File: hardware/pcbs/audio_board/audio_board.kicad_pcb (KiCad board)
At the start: 4 copper layers, 152 x 117.3 mm, 135 parts, among them J1 I2C, J10 Stereo Line-in, J2 Conn_01x08, J3 NC3MAH, J4 AudioJack3, J5 NC3MAH, J6 NC3FAH1, J7 NC3FAH1, J8 NC3FAH1, J9 DECT, Q1 S8050, Q6 2N7002, Q7 SI2309CDS-T1-GE3, U2 LP5907MFX-3.3, U3 LM5158, U4 TAD5242, U5 TAD5242, U6 TAA3040

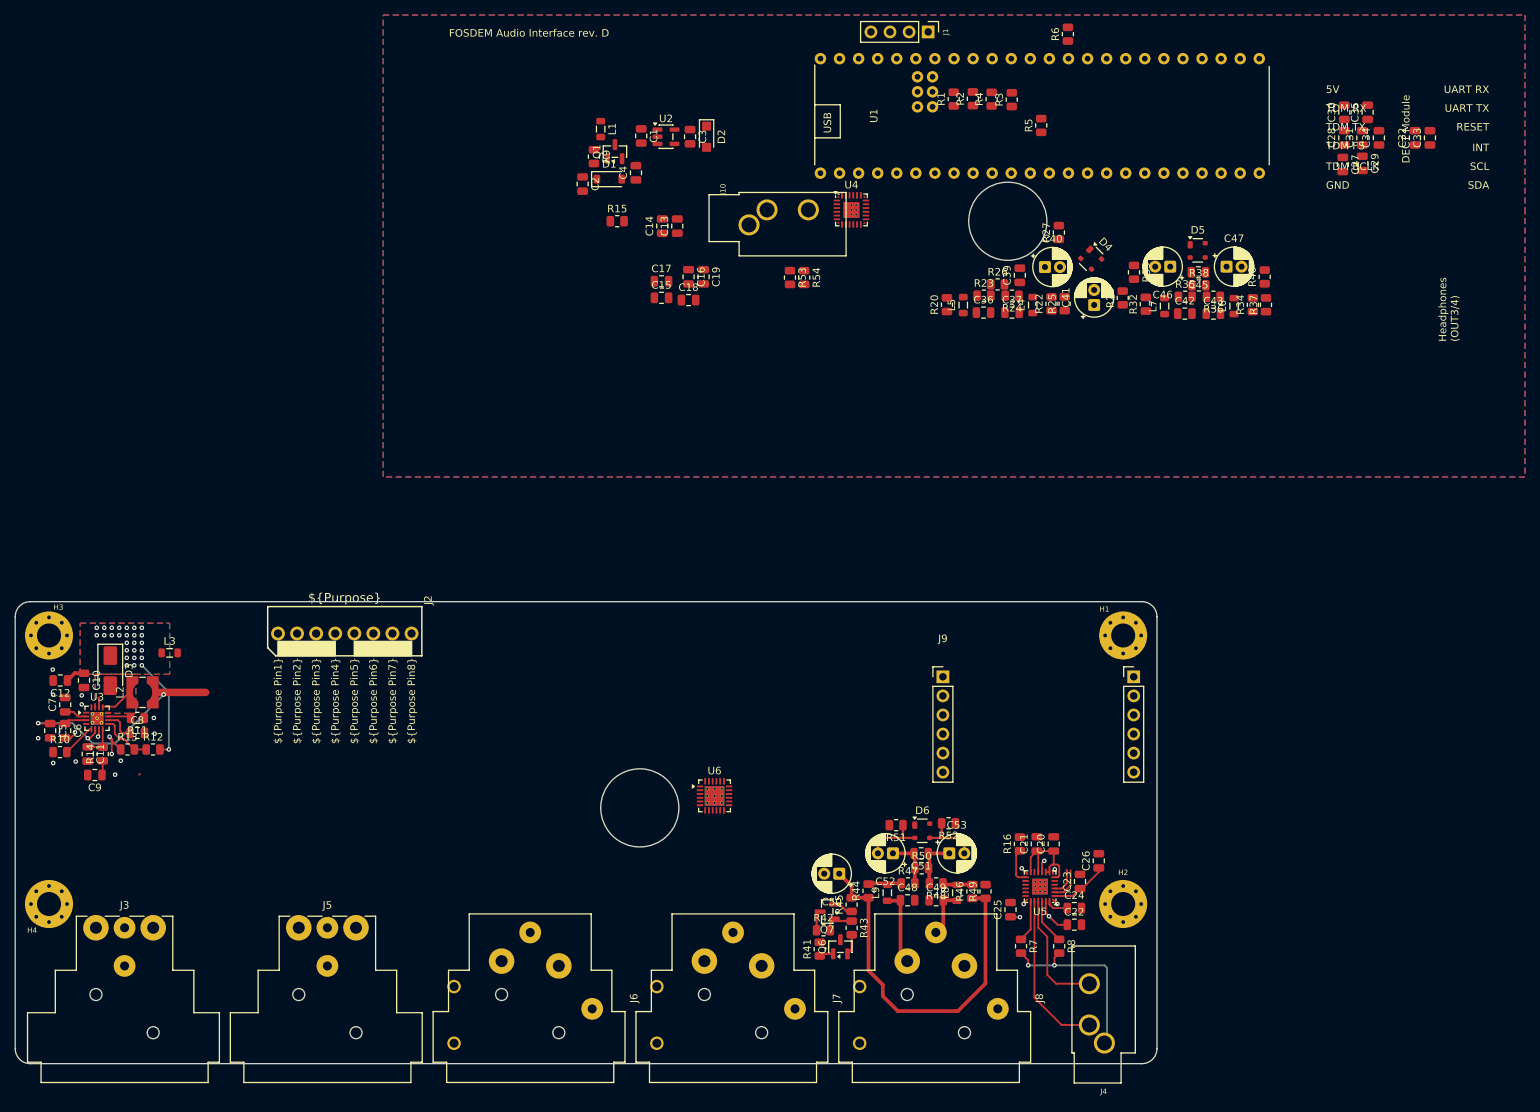
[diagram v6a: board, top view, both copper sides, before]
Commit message: route all ADC inputs
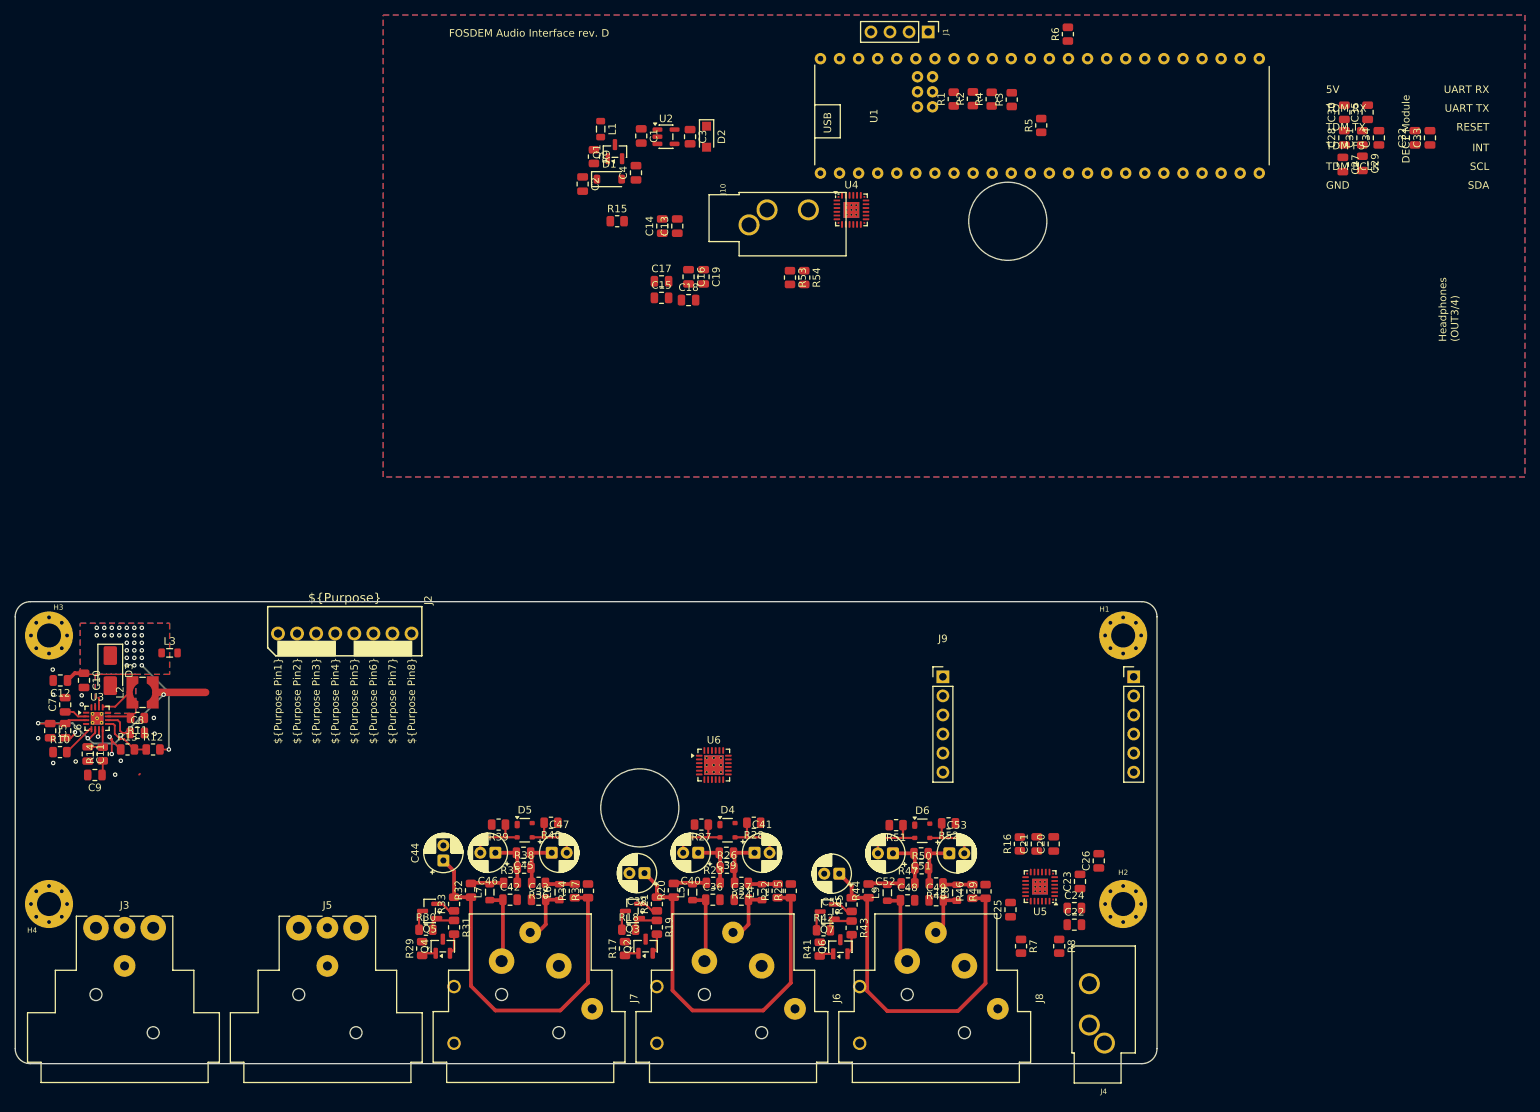
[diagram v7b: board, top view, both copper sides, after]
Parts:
- added C38: 10μF 100V, Capacitor_THT:CP_Radial_D5.0mm_P2.00mm, F.Cu at (154.0, 124.9)
- added C44: 10μF 100V, Capacitor_THT:CP_Radial_D5.0mm_P2.00mm, F.Cu at (127.2, 123.2)
- added Q2: 2N7002, Package_TO_SOT_SMD:SOT-23, F.Cu at (154.2, 134.6)
- added Q3: SI2309CDS-T1-GE3, Package_TO_SOT_SMD:SOT-23, F.Cu at (152.4, 129.9)
- added Q4: 2N7002, Package_TO_SOT_SMD:SOT-23, F.Cu at (127.2, 134.6)
- added Q5: SI2309CDS-T1-GE3, Package_TO_SOT_SMD:SOT-23, F.Cu at (125.4, 129.9)
- added R17: 10kΩ, Resistor_SMD:R_0805_2012Metric, F.Cu at (151.4, 134.9)
- added R18: 22kΩ, Resistor_SMD:R_0805_2012Metric, F.Cu at (151.9, 132.4)
- added R19: 100kΩ, Resistor_SMD:R_0805_2012Metric, F.Cu at (155.7, 132.1)
- added R21: 470Ω, Resistor_SMD:R_0805_2012Metric, F.Cu at (155.7, 129.0)
- added R29: 10kΩ, Resistor_SMD:R_0805_2012Metric, F.Cu at (124.4, 134.9)
- added R30: 22kΩ, Resistor_SMD:R_0805_2012Metric, F.Cu at (124.9, 132.4)
- added R31: 100kΩ, Resistor_SMD:R_0805_2012Metric, F.Cu at (128.7, 132.1)
- added R33: 470Ω, Resistor_SMD:R_0805_2012Metric, F.Cu at (128.7, 129.0)
- moved R40 119.6 mm to (141.6, 118.2), turned to 180 degrees
- moved R34 119.3 mm to (144.8, 127.2)
- moved R37 119.3 mm to (146.5, 127.2)
- moved C42 119.0 mm to (136.1, 128.4)
- moved C43 119.0 mm to (139.9, 128.4)
- moved C46 119.0 mm to (134.2, 122.2)
- moved C47 119.0 mm to (141.7, 122.2)
- moved L6 119.0 mm to (142.7, 127.4)
- moved L7 119.0 mm to (133.4, 127.4)
- moved R32 119.0 mm to (130.9, 127.2)
- moved R35 119.0 mm to (136.2, 126.2)
- moved R36 119.0 mm to (139.9, 126.2)
- moved R38 118.7 mm to (138.0, 124.2)
- moved C45 118.5 mm to (137.9, 122.2)
- moved D5 118.3 mm to (138.1, 119.2)
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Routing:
- net Net-(C44-Pad1): track 0.00 -> 51.3 mm
- net Net-(C38-Pad1): track 0.00 -> 50.3 mm
- net Net-(J4-PadS): track 24.7 -> 0.00 mm, vias 2 -> 0
- net /HP_L: track 21.7 -> 0.00 mm
- net /HP_R: track 16.4 -> 0.00 mm
- net +3.3V: track 15.0 -> 0.00 mm
- net +3.3VA: track 10.3 -> 0.00 mm, vias 2 -> 0
- net Net-(C42-Pad1): track 0.00 -> 10.0 mm
- net Net-(C36-Pad1): track 0.00 -> 8.98 mm
- net /ADC/IN2+: track 0.00 -> 8.14 mm
- net /ADC/IN1+: track 0.00 -> 8.14 mm
- net /ADC/IN2-: track 0.00 -> 8.08 mm
- net /ADC/IN1-: track 0.00 -> 8.08 mm
- net Net-(U5-DREG): track 7.74 -> 0.00 mm
- net Net-(C43-Pad2): track 0.00 -> 7.63 mm
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
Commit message: some more routing
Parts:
- added R9: 0, Resistor_SMD:R_0805_2012Metric, F.Cu at (208.5, 146.2)
- R7, R8: value 47 -> 0
- moved U4 126.5 mm to (96.0, 129.8), turned to 180 degrees
- moved R16 106.2 mm to (92.0, 126.8), turned to 90 degrees
- moved C15 105.7 mm to (97.8, 136.2)
- moved C18 105.6 mm to (97.8, 134.0)
- moved C13 104.7 mm to (98.0, 124.3)
- moved C14 104.7 mm to (96.0, 124.3)
- moved C17 104.3 mm to (101.0, 134.5), turned to -90 degrees
- moved C16 103.7 mm to (101.5, 131.2), turned to 0 degrees
- moved C19 101.7 mm to (103.5, 128.8), turned to 0 degrees
- moved U1 90.4 mm to (136.2, 100.1)
- moved U6 6.56 mm to (169.3, 113.0)
- moved R8 1.48 mm to (207.8, 134.6)
- moved C20 0.75 mm to (208.5, 121.8)
- moved C21 0.75 mm to (206.2, 121.8)
- moved R17 0.75 mm to (204.0, 121.8)
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- renumbered R9 to R10, R10 to R11, R11 to R12, R12 to R13, R13 to R14, R14 to R15, R15 to R16, R16 to R17, R17 to R18, R18 to R19, R19 to R20, R20 to R21, R21 to R22, R22 to R23, R23 to R24, R24 to R25, R25 to R26, R26 to R27, R27 to R28, R28 to R29, R29 to R30, R30 to R31, R31 to R32, R32 to R33, R33 to R34, R34 to R35, R35 to R36, R36 to R37, R37 to R38, R38 to R39, R39 to R40, R40 to R41, R41 to R42, R42 to R43, R43 to R44, R44 to R45, R45 to R46, R46 to R47, R47 to R48, R48 to R49, R49 to R50, R50 to R51, R51 to R52, R52 to R53, R53 to R54, R54 to R55
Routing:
- net /DAC 1/OUTB+: track 0.00 -> 29.4 mm
- net /DAC 1/OUTB-: track 0.00 -> 24.4 mm
- net +3.3VA: track 0.00 -> 22.6 mm, vias 0 -> 3
- net +3.3V: track 0.00 -> 19.1 mm
- net /HP_L: track 0.00 -> 18.9 mm
- net Net-(J4-PadS): track 0.00 -> 18.7 mm
- net /HP_R: track 0.00 -> 15.4 mm
- net /DAC 1/OUTA-: track 0.00 -> 14.2 mm
- net GND: track 7.50 -> 18.0 mm, vias 15 -> 24
- net /I2S1_BCLK: track 0.00 -> 9.57 mm
- net Net-(U5-DREG): track 0.00 -> 8.12 mm
- net /DAC 1/OUTA+: track 0.00 -> 8.00 mm
- net /I2S1_LRCLK: track 0.00 -> 7.98 mm
- net Net-(U4-DREG): track 0.00 -> 6.07 mm
- net /DAC 1/DOUT: track 0.00 -> 6.03 mm
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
